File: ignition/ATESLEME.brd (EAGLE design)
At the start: 30.3 x 53.7 mm, 54 parts, among them U1 ADXL345PATRICK, U3 AMS1117-3.3

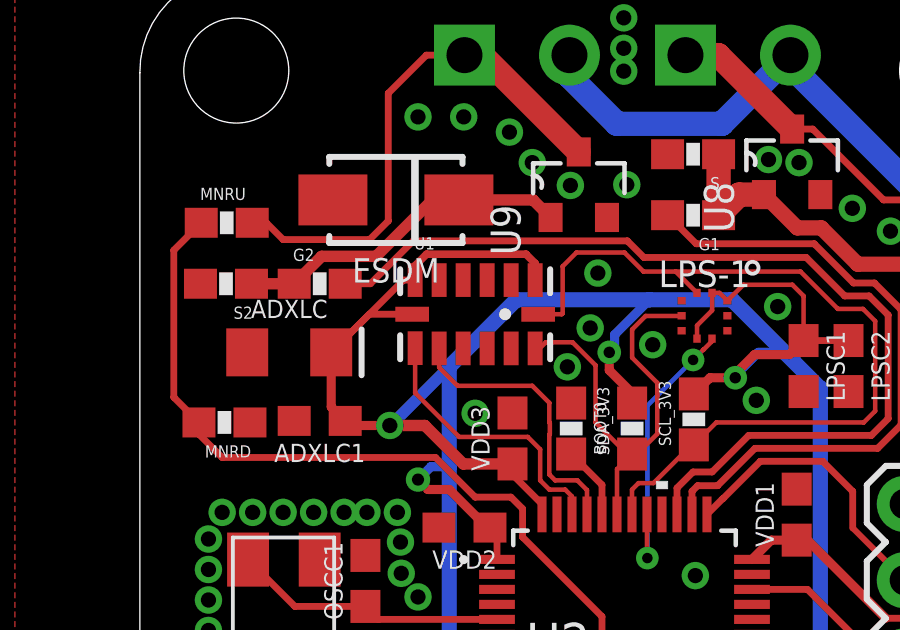
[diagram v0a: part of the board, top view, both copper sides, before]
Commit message: some modification was maken on the routes
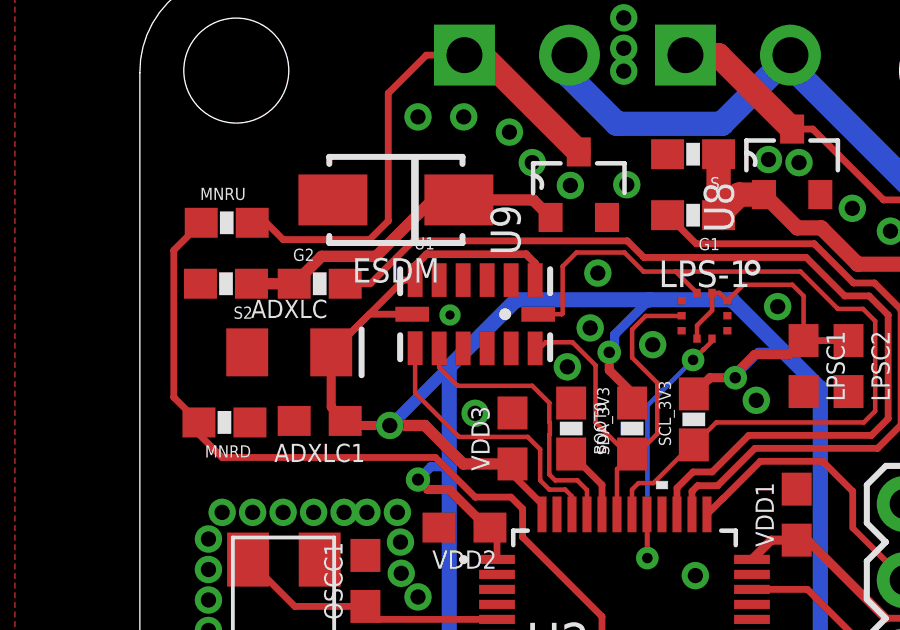
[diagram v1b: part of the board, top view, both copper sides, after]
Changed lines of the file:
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@@
 <via x="15.3416" y="39.878" extent="1-16" drill="0.508"/>
 <via x="22.6822" y="34.4678" extent="1-16" drill="0.508"/>
-<wire x1="27.9146" y1="46.7106" x2="29.1846" y2="45.9486" width="0" layer="19" extent="1-1"/>
-<wire x1="26.8478" y1="47.1678" x2="27.9146" y2="46.7106" width="0" layer="19" extent="1-1"/>
-<wire x1="26.1366" y1="48.2346" x2="26.8478" y2="47.1678" width="0" layer="19" extent="1-1"/>
-<wire x1="25.1206" y1="48.3362" x2="26.1366" y2="48.2346" width="0" layer="19" extent="1-1"/>
-<wire x1="21.756" y1="48.514" x2="25.1206" y2="48.3362" width="0" layer="19" extent="1-1"/>
-<wire x1="20.3962" y1="47.498" x2="21.756" y2="48.514" width="0" layer="19" extent="1-1"/>
-<wire x1="19.7358" y1="46.4058" x2="20.3962" y2="47.498" width="0" layer="19" extent="1-1"/>
-<wire x1="18.5166" y1="47.4726" x2="19.7358" y2="46.4058" width="0" layer="19" extent="1-1"/>
-<wire x1="17.2466" y1="48.2346" x2="18.5166" y2="47.4726" width="0" layer="19" extent="1-1"/>
-<wire x1="16.4846" y1="49.2506" x2="17.2466" y2="48.2346" width="0" layer="19" extent="1-1"/>
-<wire x1="14.9606" y1="49.7586" x2="16.4846" y2="49.2506" width="0" layer="19" extent="1-1"/>
-<wire x1="13.4366" y1="49.7586" x2="14.9606" y2="49.7586" width="0" layer="19" extent="1-1"/>
-<wire x1="19.431" y1="44.5516" x2="19.7358" y2="46.4058" width="0" layer="19" extent="1-1"/>
-<wire x1="19.177" y1="42.7228" x2="19.431" y2="44.5516" width="0" layer="19" extent="1-1"/>
-<wire x1="18.415" y1="41.4274" x2="19.177" y2="42.7228" width="0" layer="19" extent="1-1"/>
-<wire x1="18.542" y1="40.22" x2="18.415" y2="41.4274" width="0" layer="19" extent="1-1"/>
-<wire x1="16.5416" y1="42.0419" x2="18.415" y2="41.4274" width="0" layer="19" extent="1-1"/>
-<wire x1="16.5862" y1="39.8898" x2="18.542" y2="40.22" width="0" layer="19" extent="1-1"/>
-<wire x1="15.3416" y1="39.878" x2="16.5862" y2="39.8898" width="0" layer="19" extent="1-1"/>
-<wire x1="21.2598" y1="42.164" x2="19.177" y2="42.7228" width="0" layer="19" extent="1-1"/>
-<wire x1="22.2245" y1="42.6292" x2="21.2598" y2="42.164" width="0" layer="19" extent="1-1"/>
-<wire x1="22.2245" y1="43.6292" x2="22.2245" y2="42.6292" width="0" layer="19" extent="1-1"/>
-<wire x1="23.7495" y1="42.6292" x2="22.2245" y2="42.6292" width="0" layer="19" extent="1-1"/>
-<wire x1="23.7495" y1="43.1292" x2="23.7495" y2="42.6292" width="0" layer="19" extent="1-1"/>
-<wire x1="25.4254" y1="43.434" x2="23.7495" y2="43.1292" width="0" layer="19" extent="1-1"/>
-<wire x1="16.5416" y1="44.3181" x2="16.5416" y2="42.0419" width="0" layer="19" extent="1-1"/>
-<wire x1="14.9416" y1="44.3181" x2="16.5416" y2="44.3181" width="0" layer="19" extent="1-1"/>
-<wire x1="14.1416" y1="44.3181" x2="14.9416" y2="44.3181" width="0" layer="19" extent="1-1"/>
-<wire x1="24.7142" y1="40.3098" x2="23.7495" y2="42.6292" width="0" layer="19" extent="1-1"/>
-<wire x1="26.289" y1="40.6028" x2="24.7142" y2="40.3098" width="0" layer="19" extent="1-1"/>
-<wire x1="27.7876" y1="40.6028" x2="26.289" y2="40.6028" width="0" layer="19" extent="1-1"/>
-<wire x1="20.2946" y1="51.2826" x2="21.756" y2="48.514" width="0" layer="19" extent="1-1"/>
-<wire x1="20.2946" y1="52.0446" x2="20.2946" y2="51.2826" width="0" layer="19" extent="1-1"/>
-<wire x1="20.2946" y1="53.0606" x2="20.2946" y2="52.0446" width="0" layer="19" extent="1-1"/>
-<wire x1="26.0604" y1="37.3498" x2="24.7142" y2="40.3098" width="0" layer="19" extent="1-1"/>
-<wire x1="24.57" y1="34.508" x2="26.0604" y2="37.3498" width="0" layer="19" extent="1-1"/>
-<wire x1="22.6822" y1="34.4678" x2="24.57" y2="34.508" width="0" layer="19" extent="1-1"/>
-<wire x1="29.6672" y1="36.8554" x2="26.0604" y2="37.3498" width="0" layer="19" extent="1-1"/>
-<wire x1="18.07" y1="36.508" x2="16.5862" y2="39.8898" width="0" layer="19" extent="1-1"/>
-<wire x1="31.6992" y1="40.6482" x2="27.7876" y2="40.6028" width="0" layer="19" extent="1-1"/>
-<wire x1="10.6" y1="46.99" x2="13.4366" y2="49.7586" width="0" layer="19" extent="1-1"/>
-<wire x1="14.136" y1="36.068" x2="18.07" y2="36.508" width="0" layer="19" extent="1-1"/>
-<wire x1="12.8524" y1="35.5854" x2="14.136" y2="36.068" width="0" layer="19" extent="1-1"/>
-<wire x1="12.7508" y1="36.576" x2="12.8524" y2="35.5854" width="0" layer="19" extent="1-1"/>
-<wire x1="11.7348" y1="36.576" x2="12.7508" y2="36.576" width="0" layer="19" extent="1-1"/>
-<wire x1="10.9728" y1="36.576" x2="11.7348" y2="36.576" width="0" layer="19" extent="1-1"/>
-<wire x1="9.9568" y1="36.576" x2="10.9728" y2="36.576" width="0" layer="19" extent="1-1"/>
-<wire x1="8.9408" y1="36.576" x2="9.9568" y2="36.576" width="0" layer="19" extent="1-1"/>
-<wire x1="7.9248" y1="36.576" x2="8.9408" y2="36.576" width="0" layer="19" extent="1-1"/>
-<wire x1="6.9088" y1="36.576" x2="7.9248" y2="36.576" width="0" layer="19" extent="1-1"/>
-<wire x1="6.4516" y1="35.687" x2="6.9088" y2="36.576" width="0" layer="19" extent="1-1"/>
-<wire x1="6.4516" y1="34.671" x2="6.4516" y2="35.687" width="0" layer="19" extent="1-1"/>
-<wire x1="6.4516" y1="33.655" x2="6.4516" y2="34.671" width="0" layer="19" extent="1-1"/>
-<wire x1="6.4516" y1="32.639" x2="6.4516" y2="33.655" width="0" layer="19" extent="1-1"/>
-<wire x1="6.4516" y1="31.623" x2="6.4516" y2="32.639" width="0" layer="19" extent="1-1"/>
-<wire x1="12.8778" y1="34.544" x2="12.8524" y2="35.5854" width="0" layer="19" extent="1-1"/>
-<wire x1="13.4366" y1="33.7566" x2="12.8778" y2="34.544" width="0" layer="19" extent="1-1"/>
-<wire x1="11.684" y1="35.14" x2="12.8524" y2="35.5854" width="0" layer="19" extent="1-1"/>
-<wire x1="6.4516" y1="30.353" x2="6.4516" y2="31.623" width="0" layer="19" extent="1-1"/>
-<wire x1="6.4516" y1="29.337" x2="6.4516" y2="30.353" width="0" layer="19" extent="1-1"/>
-<wire x1="7.5946" y1="29.0576" x2="6.4516" y2="29.337" width="0" layer="19" extent="1-1"/>
-<wire x1="8.7376" y1="29.0576" x2="7.5946" y2="29.0576" width="0" layer="19" extent="1-1"/>
-<wire x1="9.7536" y1="29.0576" x2="8.7376" y2="29.0576" width="0" layer="19" extent="1-1"/>
-<wire x1="10.7696" y1="29.0576" x2="9.7536" y2="29.0576" width="0" layer="19" extent="1-1"/>
-<wire x1="11.811" y1="28.9306" x2="10.7696" y2="29.0576" width="0" layer="19" extent="1-1"/>
-<wire x1="12.827" y1="28.9306" x2="11.811" y2="28.9306" width="0" layer="19" extent="1-1"/>
-<wire x1="12.9286" y1="30.0482" x2="12.827" y2="28.9306" width="0" layer="19" extent="1-1"/>
-<wire x1="12.8778" y1="30.988" x2="12.9286" y2="30.0482" width="0" layer="19" extent="1-1"/>
-<wire x1="13.6144" y1="31.7754" x2="12.8778" y2="30.988" width="0" layer="19" extent="1-1"/>
-<wire x1="11.684" y1="30.138" x2="11.811" y2="28.9306" width="0" layer="19" extent="1-1"/>
-<wire x1="12.358" y1="27.686" x2="12.827" y2="28.9306" width="0" layer="19" extent="1-1"/>
-<wire x1="12.358" y1="26.162" x2="12.358" y2="27.686" width="0" layer="19" extent="1-1"/>
-<wire x1="16.07" y1="31.508" x2="13.6144" y2="31.7754" width="0" layer="19" extent="1-1"/>
-<wire x1="7.835" y1="39.5732" x2="7.9248" y2="36.576" width="0" layer="19" extent="1-1"/>
-<wire x1="9.31" y1="39.624" x2="7.835" y2="39.5732" width="0" layer="19" extent="1-1"/>
-<wire x1="7.744" y1="41.91" x2="7.835" y2="39.5732" width="0" layer="19" extent="1-1"/>
-<wire x1="6.1858" y1="44.196" x2="7.744" y2="41.91" width="0" layer="19" extent="1-1"/>
-<wire x1="15.748" y1="26.328" x2="12.358" y2="26.162" width="0" layer="19" extent="1-1"/>
-<wire x1="32.3342" y1="32.17" x2="29.6672" y2="36.8554" width="0" layer="19" extent="1-1"/>
-<wire x1="19.05" y1="21.348" x2="15.748" y2="26.328" width="0" layer="19" extent="1-1"/>
-<wire x1="21.59" y1="24.042" x2="19.05" y2="21.348" width="0" layer="19" extent="1-1"/>
-<wire x1="24.13" y1="25.8962" x2="21.59" y2="24.042" width="0" layer="19" extent="1-1"/>
-<wire x1="25.654" y1="25.8962" x2="24.13" y2="25.8962" width="0" layer="19" extent="1-1"/>
-<wire x1="22.57" y1="28.008" x2="24.13" y2="25.8962" width="0" layer="19" extent="1-1"/>
-<wire x1="23.316" y1="20.066" x2="21.59" y2="24.042" width="0" layer="19" extent="1-1"/>
-<wire x1="27.266" y1="12.446" x2="23.316" y2="20.066" width="0" layer="19" extent="1-1"/>
-<wire x1="28.574" y1="9.144" x2="27.266" y2="12.446" width="0" layer="19" extent="1-1"/>
-<wire x1="25.654" y1="3.556" x2="28.574" y2="9.144" width="0" layer="19" extent="1-1"/>
-<wire x1="18.03" y1="9.863" x2="27.266" y2="12.446" width="0" layer="19" extent="1-1"/>
-<wire x1="13.12" y1="10.668" x2="18.03" y2="9.863" width="0" layer="19" extent="1-1"/>
-<wire x1="11.812" y1="7.62" x2="13.12" y2="10.668" width="0" layer="19" extent="1-1"/>
-<wire x1="9.652" y1="8.294" x2="11.812" y2="7.62" width="0" layer="19" extent="1-1"/>
+<via x="14.5034" y="43.1546" extent="1-16" drill="0.3048"/>
 </signal>
 <signal name="VCC">

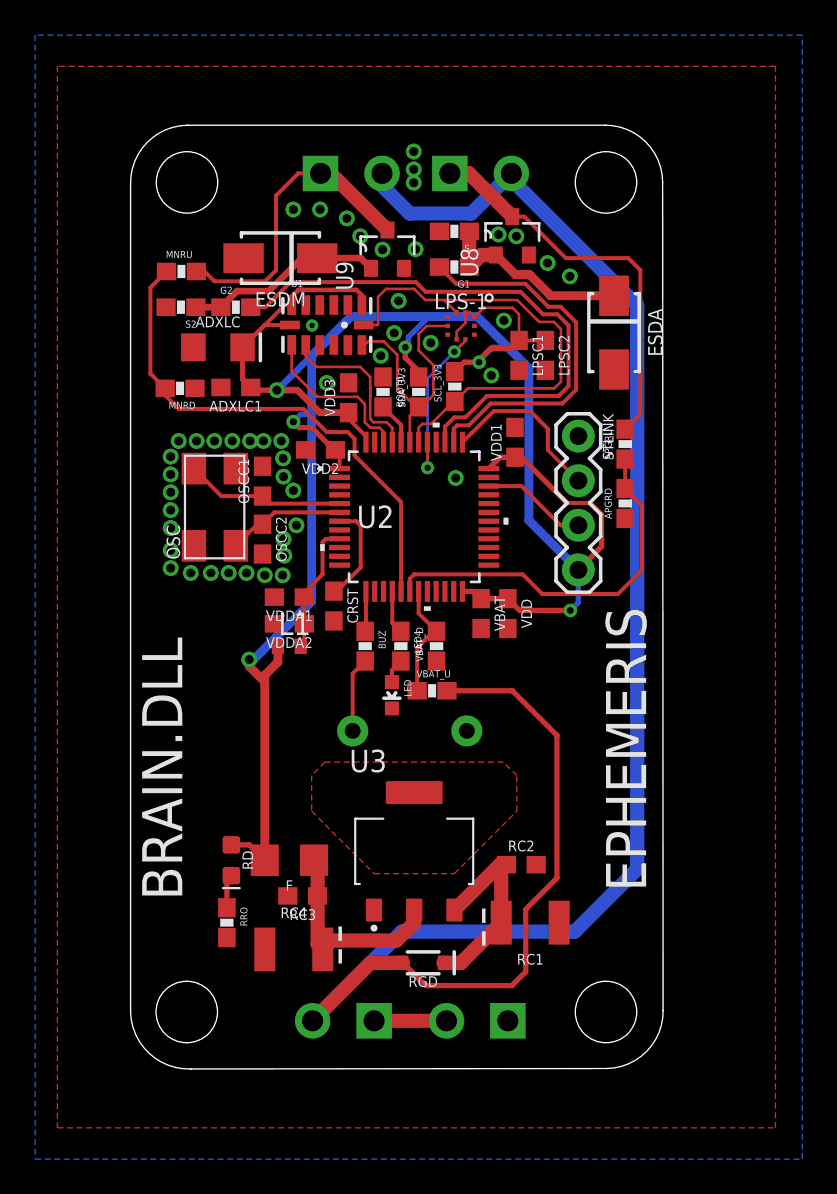
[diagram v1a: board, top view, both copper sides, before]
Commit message: Routes are be extended
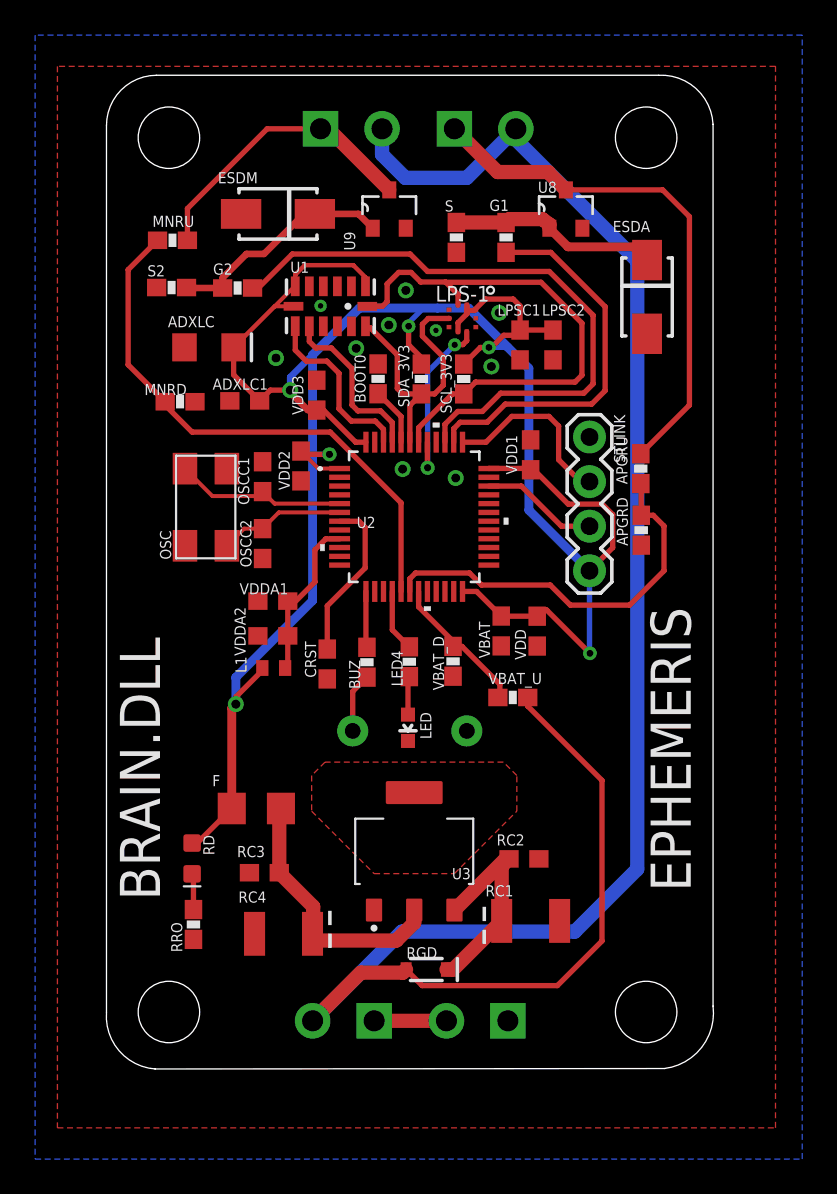
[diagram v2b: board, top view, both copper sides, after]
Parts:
- moved VBAT_U 4.61 mm to (25.9, 22.0)
- moved F 3.49 mm to (11.3, 15.6)
- moved U8 3.41 mm to (29.0, 49.8)
- moved G1 3.39 mm to (25.5, 48.2), turned to 270 degrees
- moved CRST 3.32 mm to (15.4, 23.9)
- moved ESDA 2.77 mm to (33.6, 44.8)
- moved RC3 2.55 mm to (11.8, 12.0)
- moved APOGEE 2.55 mm to (22.6, 54.4)
- moved MAIN 2.54 mm to (15.0, 54.4)
- moved ESDM 2.52 mm to (12.6, 49.5)
- moved U9 2.29 mm to (18.9, 49.8)
- moved RD 2.24 mm to (7.67, 12.8)
- moved LED 2.07 mm to (20.0, 20.2)
- moved VDD 1.94 mm to (27.3, 25.7)
- moved RRO 1.91 mm to (7.75, 9.04)
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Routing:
- net VAPG: track 22.5 -> 30.1 mm
- net 3.3V: track 133.8 -> 139.3 mm
- net MN: track 32.0 -> 36.0 mm
- net NRST: track 5.77 -> 9.43 mm
- net N$1: track 11.8 -> 15.1 mm
- net SCL_3V3: track 28.0 -> 30.7 mm
- net VIN: track 110.2 -> 112.6 mm
- net VMNS: track 29.4 -> 31.7 mm
- net VDDA: track 7.49 -> 9.37 mm
- net VSENS: track 6.58 -> 8.30 mm
- net N$8: track 11.4 -> 13.0 mm
- net LED: track 2.47 -> 3.56 mm
- net VAPGS: track 21.8 -> 22.8 mm
- net SDA_3V3: track 15.0 -> 16.0 mm
- net BUZZER: track 2.31 -> 3.20 mm
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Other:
- board size 30.3 x 53.7 mm -> 34.6 x 56.6 mm
